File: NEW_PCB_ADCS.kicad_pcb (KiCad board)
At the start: 6 copper layers, 42 x 42 mm, 79 parts, among them IC1 DRV8212DSGR, IC2 DRV8212DSGR, IC3 DRV8212DSGR, J1 SWD, J2 PANEL1, J3 PANEL2, J4 PANEL3, J5 PANEL4, J6 MTQZ, J7 Micro_SD_Card_Det_Hirose_DM3AT, U1 AD8603, U2 47K, U3 STM32L476RGTx, U4 TCAN334, U5 LIS3MDL, U6 BNO055, Y1 Crystal

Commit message: Cleanup a few things
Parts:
- removed FID1, FID2, FID3, FID4: Fiducial, Fiducial:Fiducial_0.5mm_Mask1.5mm
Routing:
- net Net-(U6-~{BOOT_LOAD_PIN}): track 14661.9 -> 3.07 mm, vias 3 -> 0
- net /PQ Bus/D-: track 41.7 -> 39.0 mm
- net GND: track 75.0 -> 73.5 mm
- net /PQ Bus/D+: track 18.3 -> 17.3 mm
- net +3V3: track 149.6 -> 148.7 mm
- net VCCQ: track 87.1 -> 86.3 mm
- net /Data Logging/CMD: track 44.1 -> 43.4 mm
- net /Data Logging/D1: track 52.2 -> 51.5 mm
- net /MCU/MTQ1-: track 7.90 -> 7.27 mm
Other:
- copper layers 6 -> 2

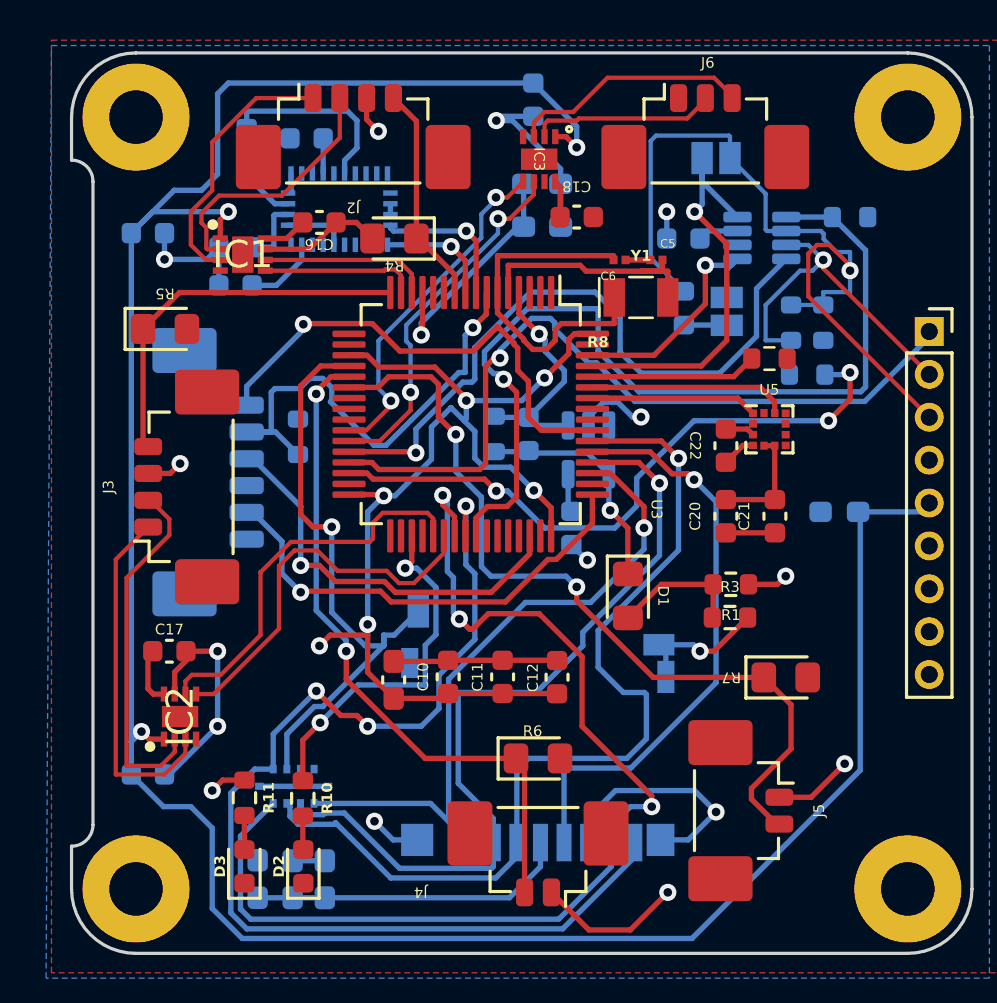
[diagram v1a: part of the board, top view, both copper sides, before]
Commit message: most unconnected items are connected
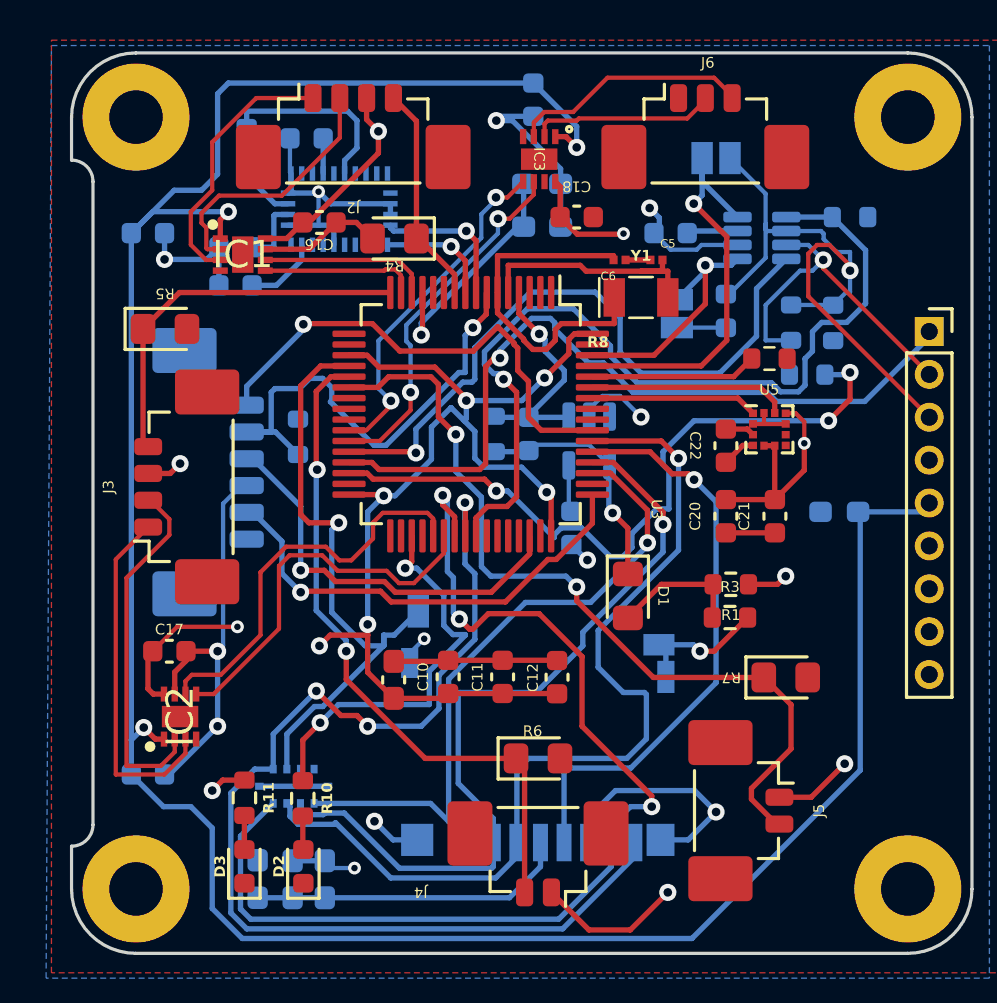
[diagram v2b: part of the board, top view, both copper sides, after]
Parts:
- moved JP2 2.33 mm to (201.4, 60.8)
- moved D4 1.96 mm to (203.7, 60.6)
- moved C19 0.65 mm to (201.1, 57.0)
- moved R13 0.46 mm to (208.7, 61.2)
- moved U1 0.41 mm to (197.3, 66.7)
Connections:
- C16 pad 1: +3V3 -> VCCQ
- C17 pad 1: +3V3 -> VCCQ
- C18 pad 1: +3V3 -> VCCQ
- C20 pad 2: +3V3 -> VCCQ
- C21 pad 2: +3V3 -> VCCQ
- C24 pad 1: +3V3 -> VCCQ
- C25 pad 1: +3V3 -> VCCQ
- IC1 pad 8: +3V3 -> VCCQ
- IC2 pad 8: +3V3 -> VCCQ
- IC3 pad 8: +3V3 -> VCCQ
- R16 pad 1: +3V3 -> VCCQ
- U5 pad 10: +3V3 -> VCCQ
- U5 pad 5: +3V3 -> VCCQ
- U5 pad 6: +3V3 -> VCCQ
- U6 pad 11: +3V3 -> VCCQ
- U6 pad 28: +3V3 -> VCCQ
- U6 pad 3: +3V3 -> VCCQ
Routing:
- net VCCQ: track 86.3 -> 133.5 mm, vias 13 -> 16
- net GND: track 73.5 -> 100.6 mm, vias 10 -> 13
- net +3V3: track 148.7 -> 122.0 mm
- net /PQ Bus/D-: track 39.0 -> 30.3 mm
- net /MCU/PB11|SDA|RX: track 30.1 -> 33.3 mm
- net /MCU/LED: track 16.9 -> 19.0 mm
- net /MCU/CAN1_EN: track 42.8 -> 40.9 mm
- net /Data Logging/SD_DET: track 28.3 -> 28.9 mm
- net /Data Logging/D3: track 38.7 -> 38.1 mm
- net /MCU/MTQ2+: track 18.5 -> 19.0 mm

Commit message: fix mistake
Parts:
- added FID1: Fiducial, Fiducial:Fiducial_0.5mm_Mask1.5mm, F.Cu at (225.2, 61.2)
- added FID2: Fiducial, Fiducial:Fiducial_0.5mm_Mask1.5mm, F.Cu at (225.2, 64.3)
- added FID3: Fiducial, Fiducial:Fiducial_0.5mm_Mask1.5mm, F.Cu at (225.2, 67.3)
- added FID4: Fiducial, Fiducial:Fiducial_0.5mm_Mask1.5mm, F.Cu at (225.2, 70.4)
- added J8: PQ9-Connector, Connector_PinSocket_2.00mm:PinSocket_1x09_P2.00mm_Vertical, F.Cu at (219.7, 61.8)
- C7, C8: moved to F.Cu
- moved C12 39.8 mm to (158.2, 64.7)
- moved C9 39.8 mm to (150.6, 64.8)
- moved C11 39.8 mm to (155.7, 64.7)
- moved R4 11.9 mm to (176.4, 56.4)
- moved C10 9.39 mm to (184.6, 70.6), turned to 180 degrees
- moved C8 5.66 mm to (190.4, 57.8)
- moved C7 4.76 mm to (190.4, 56.2)
- moved C5 0.40 mm to (200.5, 57.9)
- moved C6 0.40 mm to (198.8, 57.9)
- moved Y1 0.40 mm to (199.8, 59.6)
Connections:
- C16 pad 1: VCCQ -> +3V3
- C17 pad 1: VCCQ -> +3V3
- C18 pad 1: VCCQ -> +3V3
- C20 pad 2: VCCQ -> +3V3
- C21 pad 2: VCCQ -> +3V3
- C24 pad 1: VCCQ -> +3V3
- C25 pad 1: VCCQ -> +3V3
- IC1 pad 8: VCCQ -> +3V3
- IC2 pad 8: VCCQ -> +3V3
- IC3 pad 8: VCCQ -> +3V3
- R16 pad 1: VCCQ -> +3V3
- U5 pad 10: VCCQ -> +3V3
- U5 pad 5: VCCQ -> +3V3
- U5 pad 6: VCCQ -> +3V3
- U6 pad 11: VCCQ -> +3V3
- U6 pad 28: VCCQ -> +3V3
- U6 pad 3: VCCQ -> +3V3
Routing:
- net +3V3: track 122.0 -> 159.8 mm, vias 3 -> 6
- net VCCQ: track 133.5 -> 99.1 mm, vias 16 -> 12
- net /Data Logging/SD_DET: track 28.9 -> 0.00 mm, vias 1 -> 0
- net Net-(U3-PH1): track 16.5 -> 8.54 mm
- net /IMU/SCL_IMU: track 6.78 -> 0.00 mm, vias 1 -> 0
- net /IMU/SDA_IMU: track 5.47 -> 0.00 mm, vias 1 -> 0
- net GND: track 100.6 -> 104.7 mm
- net /Connectors/LIGHT_1: track 10.3 -> 13.0 mm
- net /Data Logging/D0: track 51.8 -> 49.2 mm
- net /MCU/JTDO: track 23.0 -> 21.6 mm
- net /Connectors/LIGHT_4: track 38.2 -> 37.4 mm

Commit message: Fix some issues
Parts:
- removed PQ9: PQ9-Connector, Connector_PinSocket_2.00mm:PinSocket_1x09_P2.00mm_Vertical
- C5, C6: footprint Library1:CAPC0603X33N -> Capacitor_SMD:C_0603_1608Metric
- R9: moved to F.Cu
- moved C12 42.7 mm to (200.8, 61.6), turned to 0 degrees
- moved C9 33.0 mm to (183.6, 66.4), turned to -90 degrees
- moved C11 28.0 mm to (183.6, 63.2)
- moved J8 6.45 mm to (213.2, 61.6)
- moved R9 5.65 mm to (181.8, 61.2), turned to 90 degrees
- moved R4 3.05 mm to (177.6, 59.2), turned to 0 degrees
- moved C5 1.34 mm to (201.8, 57.7)
- moved C13 1.05 mm to (177.8, 57.0)
- moved JP1 0.50 mm to (203.2, 54.0)
- moved C6 0.15 mm to (198.8, 57.7)
- moved R5 0.05 mm to (177.6, 61.5)
- turned C10 to 0 degrees
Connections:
- C13 pad 2: +3V3 -> +3.3VP
- C14 pad 2: +3V3 -> +3.3VP
- C15 pad 2: +3V3 -> +3.3VP
- C16 pad 1: +3V3 -> VCCQ
- C17 pad 1: +3V3 -> VCCQ
- C18 pad 1: +3V3 -> VCCQ
- C20 pad 2: +3V3 -> VCCQ
- C21 pad 2: +3V3 -> VCCQ
- C24 pad 1: +3V3 -> VCCQ
- C25 pad 1: +3V3 -> VCCQ
- FB1 pad 2: +3V3 -> +3.3VP
- IC1 pad 1: +3V3 -> +3.3VP
- IC1 pad 8: +3V3 -> VCCQ
- IC2 pad 1: +3V3 -> +3.3VP
- IC2 pad 8: +3V3 -> VCCQ
- IC3 pad 1: +3V3 -> +3.3VP
- IC3 pad 8: +3V3 -> VCCQ
- J2 pad MP: (no net) -> GND
- J3 pad MP: (no net) -> GND
- J8 pad 5: +3V3 -> +3.3VP
- R16 pad 1: +3V3 -> VCCQ
- U5 pad 10: +3V3 -> VCCQ
- U5 pad 5: +3V3 -> VCCQ
- U5 pad 6: +3V3 -> VCCQ
- U6 pad 11: +3V3 -> VCCQ
- U6 pad 28: +3V3 -> VCCQ
- U6 pad 3: +3V3 -> VCCQ
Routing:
- net +3V3: track 159.8 -> 0.00 mm, vias 6 -> 0
- net +3.3VP: track 0.00 -> 59.8 mm, vias 0 -> 3
- net VCCQ: track 99.1 -> 140.4 mm, vias 12 -> 21
- net GND: track 104.7 -> 141.0 mm, vias 13 -> 20
- net /Data Logging/SD_DET: track 0.00 -> 25.1 mm, vias 0 -> 1
- net /Connectors/LIGHT_1: track 13.0 -> 37.9 mm, vias 0 -> 2
- net /IMU/SCL_IMU: track 0.00 -> 15.0 mm, vias 0 -> 1
- net /IMU/SDA_IMU: track 0.00 -> 7.54 mm, vias 0 -> 1
- net Net-(U3-PH0): track 12.0 -> 13.8 mm
- net /MCU/PB10|SCL|TX: track 36.0 -> 34.6 mm
- net /MCU/NRST: track 22.4 -> 21.1 mm
- net /Connectors/MQT2-: track 16.5 -> 15.4 mm
- net /MCU/CAN1RX: track 19.5 -> 20.5 mm
- net /MCU/MTQ2-: track 17.9 -> 18.9 mm
- net /Data Logging/CMD: track 43.4 -> 44.4 mm
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- added copper zone on B.Cu, net +3.3VP
- added copper zone on B.Cu, net GND

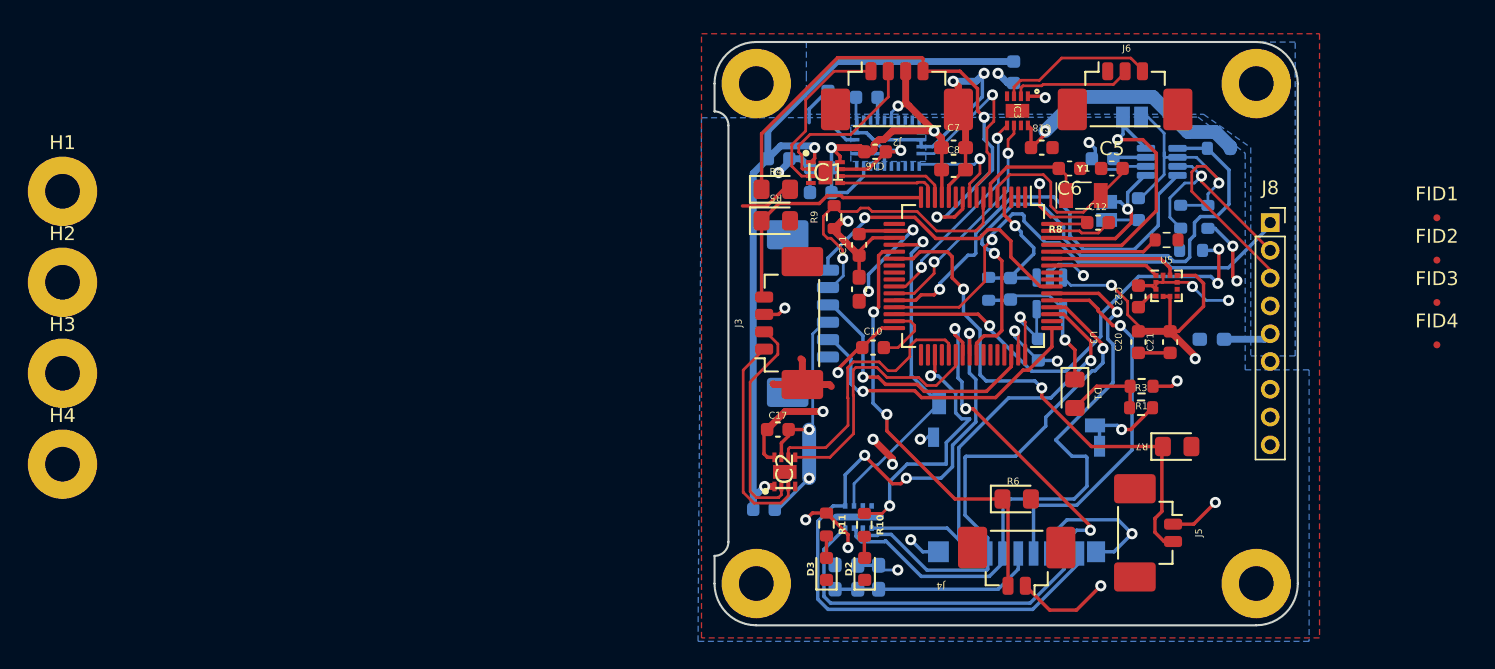
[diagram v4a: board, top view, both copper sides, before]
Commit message: Add silk screen
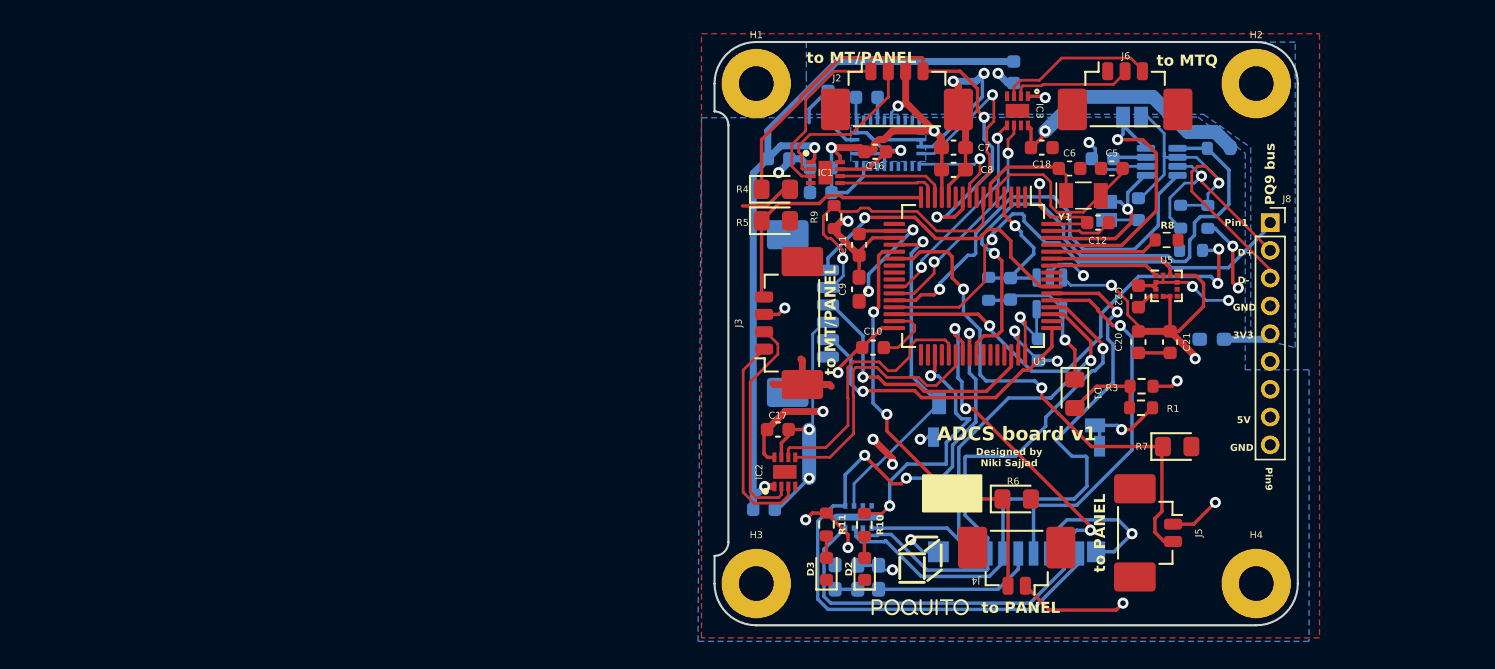
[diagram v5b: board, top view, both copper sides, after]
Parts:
- removed FID1, FID2, FID3, FID4: Fiducial, Fiducial:Fiducial_0.5mm_Mask1.5mm
- removed REF** (x4): MountingHole_2.5mm_Pad, MountingHole:MountingHole_2.5mm_Pad
- added G***: LOGO, POQUITO_Panel_Library:POQUITO-7mm, F.Cu at (188.0, 87.0)
- added G***: LOGO, POQUITO_Panel_Library:WSOF-5, B.Cu at (194.2, 88.0)
- moved H2 87.1 mm to (212.2, 51.6)
- moved H4 86.4 mm to (212.2, 87.6)
- moved H3 52.2 mm to (176.2, 87.6)
- moved H1 50.6 mm to (176.2, 51.6)
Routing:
- net VCCQ: track 140.4 -> 142.0 mm
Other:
- board text added: "3V3"
- board text added: "5V"
- board text added: "ADCS board v1"
- board text added: "D+"
- board text added: "D-"
- board text added: "Designed by Niki Sajjad"
- board text added: "GND"
- board text added: "PQ9 bus"
- board text added: "Pin1"
- board text added: "Pin9"
- board text added: "Solder jumpers for driverless CAN"
- board text added: "to MT/PANEL"
- board text added: "to MTQ"
- board text added: "to PANEL"

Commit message: Add files via upload
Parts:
- J6: footprint Connector_Molex:Molex_PicoBlade_53398-0371_1x03-1MP_P1.25mm_Vertical -> SQT-102-03-F-S:SAMTEC_SQT-102-03-F-S
- moved J6 1.12 mm to (202.3, 50.9)
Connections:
- J2 pad MP: GND -> (no net)
- J3 pad MP: GND -> (no net)
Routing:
- net /Connectors/MQT3-: track 11.1 -> 11.8 mm
